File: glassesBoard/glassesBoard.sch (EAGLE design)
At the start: 122 parts, among them J1 BM10NB(0.8)-16DS-0.4V(51), J2 DF30FC-30DS-0.4V, J3 S2B-XH-A(LF)(SN), J4 GRPB042MWCN-RC, J5 0787324001, J7 105450-0101, U10 ATTINY20-MMH, U11 SN65LVDS822VQFN48, U12 NLAS2750, U13 NX3020NAK, U14 SSM3J338RSOT-23F, U15 NX3020NAK, U16 SSM3J338RSOT-23F, U17 NX3020NAK, U18 2.8, U19 TCR2EF15SOT-25, U2 TPS613222A, U20 MICROSD, U21 MCP73833, U22 FXMA2104UMX, U23 NX3020NAK, U24 FXMA2104UMX, U25 FXMA2104UMX, U3 1.8, U4 3.3, U5 SSM3J338RSOT-23F, U6 SSM3J338RSOT-23F, U7 SN65DSI83-Q1S-PQFP-G64, U8 IQS263BDFN10, U9 NX3020NAK

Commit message: Added display connector, dip switch, 10V supply
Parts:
- added C32, C33: 100nF, thanics-capacitor:CL05A104MP5NNNC
- added C34, C35, C36: 1uF, thanics-capacitor:CL05A105MP5NNNC
- added D1: SDM03U40-7SC79, glasses:SDM03U40-7SC79
- added J6: FH26W-39S-0.3SHW, thanics-connector:FH26W-39S-0.3SHW
- added S1: 218-4LPST, glasses:218-4LPST
- added U26: LM2665M6XSOT23-6, glasses:LM2665M6XSOT23-6
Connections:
- removed net !TOUCH_INT: R39.1, U8.RDY
- new net +10V: C35.1, D1.C, J6.4, U26.OUT
- new net B0: J6.38, U11.D12
- new net B1: J6.37, U11.D13
- new net B2: J6.36, U11.D14
- new net B3: J6.35, U11.D15
- new net B4: J6.34, U11.D16
- new net B5: J6.33, U11.D17
- new net B6: J6.30, U11.D25
- new net B7: J6.29, U11.D26
- new net CABC: J6.32
- new net CLKX: J6.23, U11.CLKOUT
- new net COM: C32.1, J6.2
- new net CSTN: C33.1, J6.3
- new net DE: J6.24, U11.D20
- new net G0: J6.28, U11.D6
- new net G1: J6.27, U11.D7
- new net G2: J6.26, U11.D8
- new net G3: J6.25, U11.D9
- new net G4: J6.21, U11.D10
- new net G5: J6.20, U11.D11
- new net G6: J6.19, U11.D23
- new net G7: J6.18, U11.D24
- new net N$38: C34.1, U26.CAP+
- new net N$40: C34.2, U26.CAP-
- new net N$42: C35.2, C36.1
- new net R0: J6.17, U11.D0
- new net R1: J6.16, U11.D1
- new net R2: J6.14, U11.D2
- new net R3: J6.13, U11.D3
- new net R4: J6.12, U11.D4
- new net R5: J6.11, U11.D5
- new net R6: J6.10, U11.D21
- new net R7: J6.9, U11.D22
- new net RESETB: J6.6
- new net SCL: J6.8
- new net SDA: J6.7
- new net TEST_HV: J6.1
- net !TOUCH_INT_1V8: now also R39.1, U8.RDY
- net +1V8: now also J6.15, J6.31, S1.3
- net +5V: now also D1.A, U26.V+
- net BOOT_CONFIG_1: now also S1.6
- net FORCED_USB_BOOT: now also S1.2
- net GND: now also C32.2, C33.2, C36.2, J6.22, J6.5, S1.7, U26.GND, U26.SD
- net N$14: now also S1.1
- net N$34: now also S1.5
- net PM_RESIN_N: now also S1.8
- net USB_HS_ID: now also S1.4
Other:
- moved on the sheet: R11, R39, R52

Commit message: more progress on routing
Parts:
- removed C30: 1uF, thanics-capacitor:CL05A105MP5NNNC
- added R50: 10k, thanics-resistor:RC0402JR-0710KL
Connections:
- removed net !SHUTDOWN_LVDS: U11.SHTDN#
- removed net LED_B: J4.4, U$1G$2.GPIO62, U$1G$2.PM_MPP3
- removed net LED_G: J4.3, U$1G$2.GPIO109, U$1G$2.PM_MPP2
- removed net LED_R: J4.5, U$1G$2.PM_MPP4
- removed net SCL: J6.8
- removed net SDA: J6.7
- net +1V5: no longer C30.1
- net +1V8: now also R50.2
- net DSI_EN: now also U$1G$1.GPIO8, U11.SHTDN#; no longer U$1G$2.GPIO118
- net GND: no longer C30.2
- net I2C3_SCL: now also J6.8
- net I2C3_SDA: now also J6.7
- net RESETB: now also R50.1
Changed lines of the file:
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@@
 <part name="U$38" library="supply1" deviceset="+1V8" device=""/>
 <part name="C29" library="thanics-capacitor" deviceset="CL05A105MP5NNNC" device="" value="1uF"/>
-<part name="C30" library="thanics-capacitor" deviceset="CL05A105MP5NNNC" device="" value="1uF"/>
 <part name="C31" library="thanics-capacitor" deviceset="CL05A105MP5NNNC" device="" value="1uF"/>
 <part name="GND61" library="supply1" library_urn="urn:adsk.eagle:library:371" deviceset="GND" device=""/>
-<part name="GND62" library="supply1" library_urn="urn:adsk.eagle:library:371" deviceset="GND" device=""/>
 <part name="GND63" library="supply1" library_urn="urn:adsk.eagle:library:371" deviceset="GND" device=""/>
 <part name="U22" library="glasses" deviceset="FXMA2104UMX" device=""/>
@@
 <part name="P+13" library="supply1" library_urn="urn:adsk.eagle:library:371" deviceset="+5V" device=""/>
 <part name="GND40" library="supply1" library_urn="urn:adsk.eagle:library:371" deviceset="GND" device=""/>
+<part name="R50" library="thanics-resistor" deviceset="RC0402JR-0710KL" device="" value="10k"/>
+<part name="U$48" library="supply1" deviceset="+1V8" device=""/>
 </parts>
 <sheets>
@@
 <attribute name="RATING" x="-44.958" y="-326.644" size="1.524" layer="95"/>
 </instance>
-<instance part="C30" gate="G$1" x="-55.88" y="-302.26" smashed="yes" rot="R270">
-<attribute name="NAME" x="-55.118" y="-299.974" size="2.032" layer="95"/>
-<attribute name="VALUE" x="-55.118" y="-303.784" size="1.524" layer="95"/>
-<attribute name="RATING" x="-55.118" y="-306.324" size="1.524" layer="95"/>
-</instance>
 <instance part="C31" gate="G$1" x="-71.12" y="-299.72" smashed="yes" rot="R270">
 <attribute name="NAME" x="-70.358" y="-297.434" size="2.032" layer="95"/>
@@
 <attribute name="VALUE" x="-48.26" y="-330.2" size="1.778" layer="96"/>
 </instance>
-<instance part="GND62" gate="1" x="-55.88" y="-307.34" smashed="yes">
-<attribute name="VALUE" x="-58.42" y="-309.88" size="1.778" layer="96"/>
-</instance>
 <instance part="GND63" gate="1" x="-71.12" y="-304.8" smashed="yes">
 <attribute name="VALUE" x="-73.66" y="-307.34" size="1.778" layer="96"/>
@@
 <attribute name="VALUE" x="-393.7" y="-101.6" size="1.778" layer="96"/>
 </instance>
+<instance part="R50" gate="G$1" x="114.3" y="-5.08" smashed="yes" rot="R90">
+<attribute name="NAME" x="112.8014" y="-8.89" size="1.778" layer="95" rot="R90"/>
+<attribute name="VALUE" x="117.602" y="-8.89" size="1.778" layer="96" rot="R90"/>
+</instance>
+<instance part="U$48" gate="G$1" x="114.3" y="2.54" smashed="yes">
+<attribute name="VALUE" x="111.76" y="0" size="1.778" layer="96" rot="R90"/>
+</instance>
 </instances>
 <busses>
@@
 </segment>
 <segment>
-<pinref part="GND62" gate="1" pin="GND"/>
-<pinref part="C30" gate="G$1" pin="2"/>
-<wire x1="-55.88" y1="-304.8" x2="-55.88" y2="-304.038" width="0.1524" layer="91"/>
-</segment>
-<segment>
 <pinref part="U23" gate="A" pin="S"/>
 <pinref part="GND64" gate="1" pin="GND"/>
@@
 <pinref part="S1" gate="G$1" pin="3"/>
 </segment>
+<segment>
+<pinref part="R50" gate="G$1" pin="2"/>
+<pinref part="U$48" gate="G$1" pin="+1V8"/>
+<wire x1="114.3" y1="0" x2="114.3" y2="2.54" width="0.1524" layer="91"/>
+</segment>
 </net>
 <net name="VBATT_IN" class="0">
@@
 <label x="-86.36" y="-43.18" size="1.778" layer="95"/>
 </segment>
+<segment>
+<pinref part="J6" gate="G$1" pin="8"/>
+<wire x1="99.06" y1="-20.32" x2="114.3" y2="-20.32" width="0.1524" layer="91"/>
+<label x="111.76" y="-20.32" size="1.778" layer="95" align="bottom-right"/>
+</segment>
 </net>
 <net name="I2C3_SDA" class="0">
@@
 <label x="-86.36" y="-45.72" size="1.778" layer="95"/>
 </segment>
+<segment>
+<pinref part="J6" gate="G$1" pin="7"/>
+<wire x1="81.28" y1="-20.32" x2="66.04" y2="-20.32" width="0.1524" layer="91"/>
+<label x="68.58" y="-20.32" size="1.778" layer="95"/>
+</segment>
 </net>
 <net name="N$16" class="0">
@@
 <net name="DSI_EN" class="0">
 <segment>
-<pinref part="U$1" gate="G$2" pin="GPIO118"/>
-<wire x1="-160.02" y1="-218.44" x2="-132.08" y2="-218.44" width="0.1524" layer="91"/>
-<label x="-149.86" y="-218.44" size="1.778" layer="95"/>
-</segment>
-<segment>
 <pinref part="U7" gate="G$1" pin="EN"/>
 <pinref part="R14" gate="G$1" pin="2"/>
@@
 <label x="-83.82" y="-50.8" size="1.778" layer="95"/>
 </segment>
+<segment>
+<pinref part="U$1" gate="G$1" pin="GPIO8"/>
+<wire x1="-220.98" y1="-99.06" x2="-246.38" y2="-99.06" width="0.1524" layer="91"/>
+<label x="-243.84" y="-99.06" size="1.778" layer="95"/>
+</segment>
+<segment>
+<pinref part="U11" gate="G$1" pin="SHTDN#"/>
+<wire x1="0" y1="-58.42" x2="-22.86" y2="-58.42" width="0.1524" layer="91"/>
+<label x="-22.86" y="-58.42" size="1.778" layer="95"/>
+</segment>
 </net>
 <net name="N$27" class="0">
@@
 <pinref part="J2" gate="G$1" pin="6"/>
 <wire x1="-81.28" y1="-309.88" x2="-60.96" y2="-309.88" width="0.1524" layer="91"/>
-<wire x1="-60.96" y1="-309.88" x2="-60.96" y2="-297.18" width="0.1524" layer="91"/>
+<wire x1="-60.96" y1="-309.88" x2="-60.96" y2="-294.64" width="0.1524" layer="91"/>
 <pinref part="U$18" gate="G$1" pin="+1V5"/>
-<pinref part="C30" gate="G$1" pin="1"/>
-<wire x1="-60.96" y1="-297.18" x2="-60.96" y2="-294.64" width="0.1524" layer="91"/>
-<wire x1="-55.88" y1="-298.196" x2="-55.88" y2="-297.18" width="0.1524" layer="91"/>
-<wire x1="-55.88" y1="-297.18" x2="-60.96" y2="-297.18" width="0.1524" layer="91"/>
-<junction x="-60.96" y="-297.18"/>
 </segment>
 <segment>
@@
 </segment>
 </net>
-<net name="LED_R" class="0">
-<segment>
-<pinref part="J4" gate="G$1" pin="5"/>
-<wire x1="-393.7" y1="-254" x2="-378.46" y2="-254" width="0.1524" layer="91"/>
-<label x="-391.16" y="-254" size="1.778" layer="95"/>
-</segment>
-<segment>
-<pinref part="U$1" gate="G$2" pin="PM_MPP4"/>
-<wire x1="-220.98" y1="-144.78" x2="-246.38" y2="-144.78" width="0.1524" layer="91"/>
-<label x="-243.84" y="-144.78" size="1.778" layer="95"/>
-</segment>
-</net>
-<net name="LED_G" class="0">
-<segment>
-<pinref part="J4" gate="G$1" pin="3"/>
-<wire x1="-414.02" y1="-251.46" x2="-431.8" y2="-251.46" width="0.1524" layer="91"/>
-<label x="-424.18" y="-251.46" size="1.778" layer="95"/>
-</segment>
-<segment>
-<pinref part="U$1" gate="G$2" pin="GPIO109"/>
-<wire x1="-220.98" y1="-210.82" x2="-246.38" y2="-210.82" width="0.1524" layer="91"/>
-<label x="-243.84" y="-210.82" size="1.778" layer="95"/>
-</segment>
-<segment>
-<pinref part="U$1" gate="G$2" pin="PM_MPP2"/>
-<wire x1="-220.98" y1="-147.32" x2="-246.38" y2="-147.32" width="0.1524" layer="91"/>
-</segment>
-</net>
-<net name="LED_B" class="0">
-<segment>
-<pinref part="J4" gate="G$1" pin="4"/>
-<wire x1="-414.02" y1="-254" x2="-431.8" y2="-254" width="0.1524" layer="91"/>
-<label x="-424.18" y="-254" size="1.778" layer="95"/>
-</segment>
-<segment>
-<pinref part="U$1" gate="G$2" pin="GPIO62"/>
-<wire x1="-220.98" y1="-213.36" x2="-246.38" y2="-213.36" width="0.1524" layer="91"/>
-<label x="-243.84" y="-213.36" size="1.778" layer="95"/>
-</segment>
-<segment>
-<pinref part="U$1" gate="G$2" pin="PM_MPP3"/>
-<wire x1="-220.98" y1="-139.7" x2="-246.38" y2="-139.7" width="0.1524" layer="91"/>
-<label x="-243.84" y="-139.7" size="1.778" layer="95"/>
-</segment>
-</net>
 <net name="N$36" class="0">
 <segment>
@@
 </segment>
 </net>
-<net name="!SHUTDOWN_LVDS" class="0">
-<segment>
-<pinref part="U11" gate="G$1" pin="SHTDN#"/>
-<wire x1="0" y1="-58.42" x2="-22.86" y2="-58.42" width="0.1524" layer="91"/>
-<label x="-22.86" y="-58.42" size="1.778" layer="95"/>
-</segment>
-</net>
 <net name="N$39" class="0">
 <segment>
@@
 </segment>
 </net>
-<net name="SDA" class="0">
-<segment>
-<pinref part="J6" gate="G$1" pin="7"/>
-<wire x1="81.28" y1="-20.32" x2="66.04" y2="-20.32" width="0.1524" layer="91"/>
-<label x="68.58" y="-20.32" size="1.778" layer="95"/>
-</segment>
-</net>
 <net name="R7" class="0">
 <segment>
@@
 </segment>
 </net>
-<net name="SCL" class="0">
-<segment>
-<pinref part="J6" gate="G$1" pin="8"/>
-<wire x1="99.06" y1="-20.32" x2="114.3" y2="-20.32" width="0.1524" layer="91"/>
-<label x="111.76" y="-20.32" size="1.778" layer="95" align="bottom-right"/>
-</segment>
-</net>
 <net name="RESETB" class="0">
 <segment>
@@
 <wire x1="99.06" y1="-17.78" x2="114.3" y2="-17.78" width="0.1524" layer="91"/>
 <label x="111.76" y="-17.78" size="1.778" layer="95" align="bottom-right"/>
+<pinref part="R50" gate="G$1" pin="1"/>
+<wire x1="114.3" y1="-17.78" x2="114.3" y2="-10.16" width="0.1524" layer="91"/>
 </segment>
 </net>

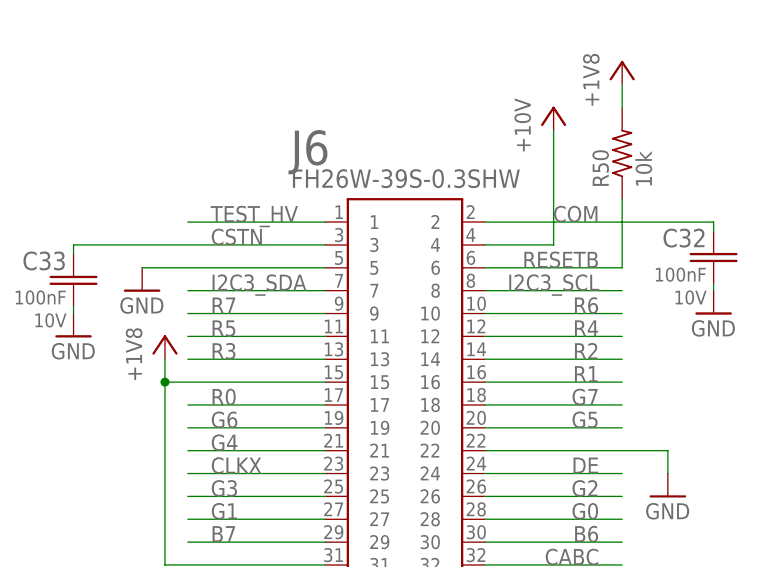
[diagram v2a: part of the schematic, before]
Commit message: made more progress on routing, and added capacitive touch slider board
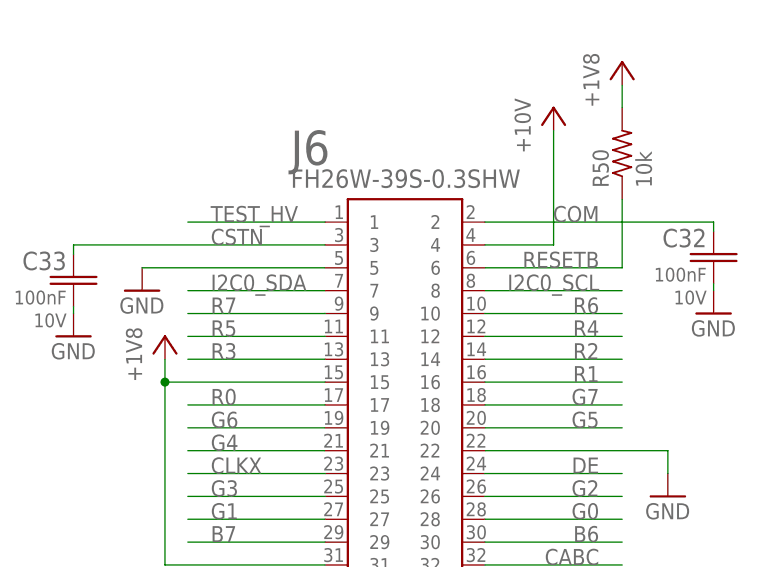
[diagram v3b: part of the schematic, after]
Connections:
- net I2C0_SCL: now also J6.8
- net I2C0_SDA: now also J6.7
- net I2C3_SCL: no longer J6.8
- net I2C3_SDA: no longer J6.7
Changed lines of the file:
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@@
 <label x="-513.08" y="-292.1" size="1.778" layer="95"/>
+</segment>
+<segment>
+<pinref part="J6" gate="G$1" pin="7"/>
+<wire x1="81.28" y1="-20.32" x2="66.04" y2="-20.32" width="0.1524" layer="91"/>
+<label x="68.58" y="-20.32" size="1.778" layer="95"/>
 </segment>
 </net>
@@
 <wire x1="-515.62" y1="-193.04" x2="-492.76" y2="-193.04" width="0.1524" layer="91"/>
 <label x="-513.08" y="-193.04" size="1.778" layer="95"/>
+</segment>
+<segment>
+<pinref part="J6" gate="G$1" pin="8"/>
+<wire x1="99.06" y1="-20.32" x2="114.3" y2="-20.32" width="0.1524" layer="91"/>
+<label x="111.76" y="-20.32" size="1.778" layer="95" align="bottom-right"/>
 </segment>
 </net>
@@
 <label x="-86.36" y="-43.18" size="1.778" layer="95"/>
 </segment>
-<segment>
-<pinref part="J6" gate="G$1" pin="8"/>
-<wire x1="99.06" y1="-20.32" x2="114.3" y2="-20.32" width="0.1524" layer="91"/>
-<label x="111.76" y="-20.32" size="1.778" layer="95" align="bottom-right"/>
-</segment>
 </net>
 <net name="I2C3_SDA" class="0">
@@
 <label x="-86.36" y="-45.72" size="1.778" layer="95"/>
 </segment>
-<segment>
-<pinref part="J6" gate="G$1" pin="7"/>
-<wire x1="81.28" y1="-20.32" x2="66.04" y2="-20.32" width="0.1524" layer="91"/>
-<label x="68.58" y="-20.32" size="1.778" layer="95"/>
-</segment>
 </net>

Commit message: about to move fingerprint sensor connector and add backlight connector
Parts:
- added R51: 8R, thanics-resistor:RMCF0402JT8R20
- added R54: 10k, thanics-resistor:RC0402JR-0710KL
- added U27: NX3020NAK, glasses:NX3020NAK
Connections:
- new net BACKLIGHT_PWM: R54.2, U$1G$2.PM_MPP4, U27.G
- new net N$41: R51.1, U27.D
- net GND: now also R54.1, U27.S
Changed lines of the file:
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@@
 <part name="R50" library="thanics-resistor" deviceset="RC0402JR-0710KL" device="" value="10k"/>
 <part name="U$48" library="supply1" deviceset="+1V8" device=""/>
+<part name="U27" library="glasses" deviceset="NX3020NAK" device=""/>
+<part name="R51" library="thanics-resistor" deviceset="RMCF0402JT8R20" device="" value="8R"/>
+<part name="+3V7" library="supply1" library_urn="urn:adsk.eagle:library:371" deviceset="+3V3" device=""/>
+<part name="GND62" library="supply1" library_urn="urn:adsk.eagle:library:371" deviceset="GND" device=""/>
+<part name="GND77" library="supply1" library_urn="urn:adsk.eagle:library:371" deviceset="GND" device=""/>
+<part name="R54" library="thanics-resistor" deviceset="RC0402JR-0710KL" device="" value="10k"/>
 </parts>
 <sheets>
@@
 <attribute name="VALUE" x="111.76" y="0" size="1.778" layer="96" rot="R90"/>
 </instance>
+<instance part="U27" gate="A" x="93.98" y="-104.14" smashed="yes">
+<attribute name="NAME" x="99.06" y="-104.14" size="1.778" layer="95" font="vector"/>
+<attribute name="PART#" x="99.06" y="-106.68" size="1.778" layer="96" font="vector"/>
+</instance>
+<instance part="R51" gate="G$1" x="93.98" y="-91.44" smashed="yes" rot="R90">
+<attribute name="NAME" x="92.4814" y="-95.25" size="1.778" layer="95" rot="R90"/>
+<attribute name="VALUE" x="97.282" y="-95.25" size="1.778" layer="96" rot="R90"/>
+</instance>
+<instance part="+3V7" gate="G$1" x="93.98" y="-76.2" smashed="yes">
+<attribute name="VALUE" x="91.44" y="-81.28" size="1.778" layer="96" rot="R90"/>
+</instance>
+<instance part="GND62" gate="1" x="93.98" y="-114.3" smashed="yes">
+<attribute name="VALUE" x="91.44" y="-116.84" size="1.778" layer="96"/>
+</instance>
+<instance part="GND77" gate="1" x="83.82" y="-124.46" smashed="yes">
+<attribute name="VALUE" x="81.28" y="-127" size="1.778" layer="96"/>
+</instance>
+<instance part="R54" gate="G$1" x="83.82" y="-114.3" smashed="yes" rot="R90">
+<attribute name="NAME" x="82.3214" y="-118.11" size="1.778" layer="95" rot="R90"/>
+<attribute name="VALUE" x="87.122" y="-118.11" size="1.778" layer="96" rot="R90"/>
+</instance>
 </instances>
 <busses>
@@
 <junction x="-396.24" y="-86.36"/>
 </segment>
+<segment>
+<pinref part="GND77" gate="1" pin="GND"/>
+<pinref part="R54" gate="G$1" pin="1"/>
+<wire x1="83.82" y1="-121.92" x2="83.82" y2="-119.38" width="0.1524" layer="91"/>
+</segment>
+<segment>
+<pinref part="GND62" gate="1" pin="GND"/>
+<pinref part="U27" gate="A" pin="S"/>
+<wire x1="93.98" y1="-111.76" x2="93.98" y2="-108.458" width="0.1524" layer="91"/>
+</segment>
 </net>
 <net name="VREG_L11_SDC" class="0">
@@
 </segment>
 </net>
+<net name="BACKLIGHT_PWM" class="0">
+<segment>
+<pinref part="U$1" gate="G$2" pin="PM_MPP4"/>
+<wire x1="-220.98" y1="-144.78" x2="-246.38" y2="-144.78" width="0.1524" layer="91"/>
+<label x="-243.84" y="-144.78" size="1.778" layer="95"/>
+</segment>
+<segment>
+<pinref part="U27" gate="A" pin="G"/>
+<wire x1="88.9" y1="-106.68" x2="83.82" y2="-106.68" width="0.1524" layer="91"/>
+<label x="68.58" y="-106.68" size="1.778" layer="95"/>
+<pinref part="R54" gate="G$1" pin="2"/>
+<wire x1="83.82" y1="-106.68" x2="66.04" y2="-106.68" width="0.1524" layer="91"/>
+<wire x1="83.82" y1="-109.22" x2="83.82" y2="-106.68" width="0.1524" layer="91"/>
+<junction x="83.82" y="-106.68"/>
+</segment>
+</net>
+<net name="N$41" class="0">
+<segment>
+<pinref part="U27" gate="A" pin="D"/>
+<pinref part="R51" gate="G$1" pin="1"/>
+<wire x1="93.98" y1="-99.822" x2="93.98" y2="-96.52" width="0.1524" layer="91"/>
+</segment>
+</net>

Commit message: finished rev 1 of design
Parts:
- added J8: 5-520315-2, thanics-connector:5-520315-2
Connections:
- new net N$43: J8.2, R51.2
- net +3V3: now also J8.1
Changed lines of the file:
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@@
 <part name="GND77" library="supply1" library_urn="urn:adsk.eagle:library:371" deviceset="GND" device=""/>
 <part name="R54" library="thanics-resistor" deviceset="RC0402JR-0710KL" device="" value="10k"/>
+<part name="J8" library="thanics-connector" deviceset="5-520315-2" device=""/>
 </parts>
 <sheets>
@@
 <attribute name="VALUE" x="87.122" y="-118.11" size="1.778" layer="96" rot="R90"/>
 </instance>
+<instance part="J8" gate="G$1" x="109.22" y="-83.82" smashed="yes">
+<attribute name="NAME" x="104.14" y="-74.93" size="3.81" layer="95"/>
+</instance>
 </instances>
 <busses>
@@
 <junction x="-2.54" y="10.16"/>
 </segment>
+<segment>
+<pinref part="J8" gate="G$1" pin="1"/>
+<pinref part="+3V7" gate="G$1" pin="+3V3"/>
+<wire x1="99.06" y1="-81.28" x2="93.98" y2="-81.28" width="0.1524" layer="91"/>
+<wire x1="93.98" y1="-81.28" x2="93.98" y2="-78.74" width="0.1524" layer="91"/>
+</segment>
 </net>
 <net name="+1V8" class="0">
@@
 </segment>
 </net>
+<net name="N$43" class="0">
+<segment>
+<pinref part="J8" gate="G$1" pin="2"/>
+<pinref part="R51" gate="G$1" pin="2"/>
+<wire x1="99.06" y1="-83.82" x2="93.98" y2="-83.82" width="0.1524" layer="91"/>
+<wire x1="93.98" y1="-83.82" x2="93.98" y2="-86.36" width="0.1524" layer="91"/>
+</segment>
+</net>
